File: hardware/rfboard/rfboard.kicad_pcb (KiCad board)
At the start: 4 copper layers, 20 x 59 mm, 62 parts, among them J1 10118194-0001LF, J2 Conn_01x04, J3 2337019-1, J4 Conn_01x02, P2 CONN_01X03, SW1 SW_Push, SW2 SW_Push, SW3 SW_Push, U1 STM32G070KBTx, U2 RFM69HCW, U3 CH340X, U4 XL-0807RGBC-WS2812B, U5 XC6206P332MR-G, U6 HX 1210-C06

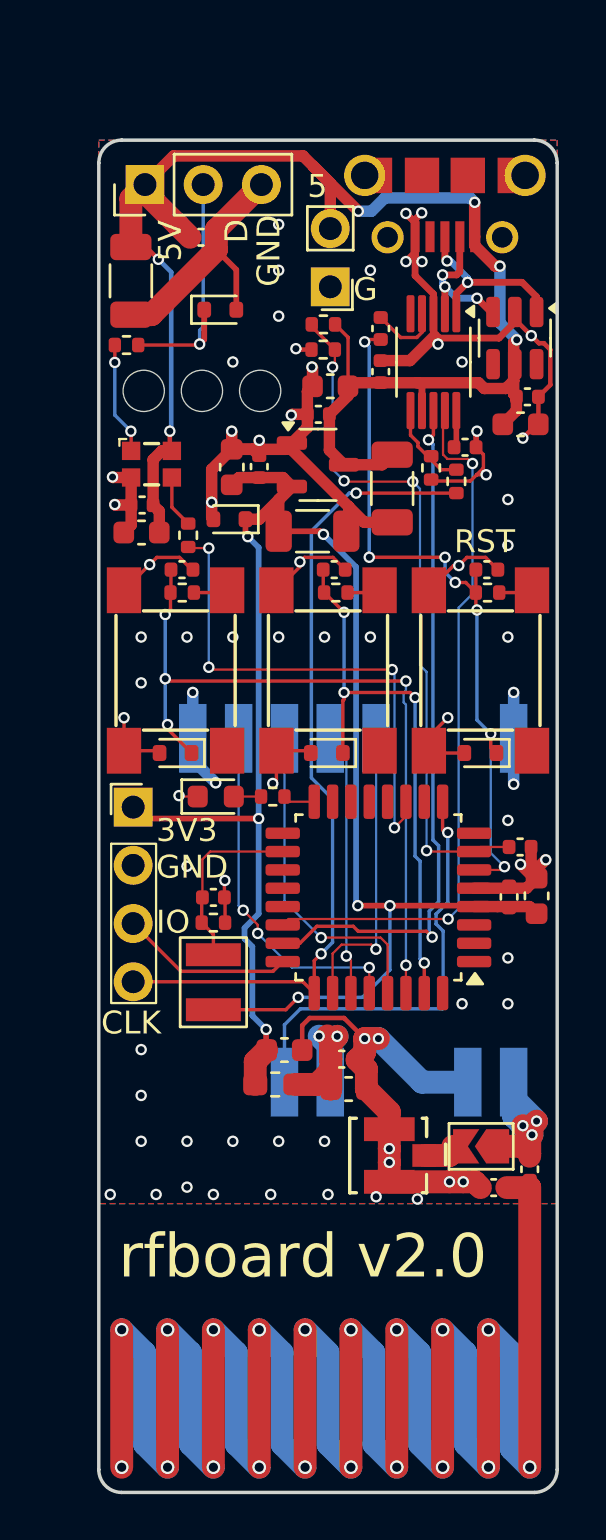
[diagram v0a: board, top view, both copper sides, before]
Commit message: Update the rfboard hardware designs for v2.1:
- Fix USB-USART connections to use the correct MCU pins
- Add thermal relief for the u.FL connector
- Switch to USB-C
- Switch to an LDO voltage regulator with a high PSRR
- Remove inner copper layers from antenna vias
- Increase antenna via copper to 1mm diameter
- Add a the 3rd pi filter footprint
- Add a 220uF electrolytic cap on the 5V rail
- Improve the decoupling story overall
- Remove the ferrite on the radio power supply

Change-Id: Iff05fab2d52248b6d165e85d5234a398977c2398
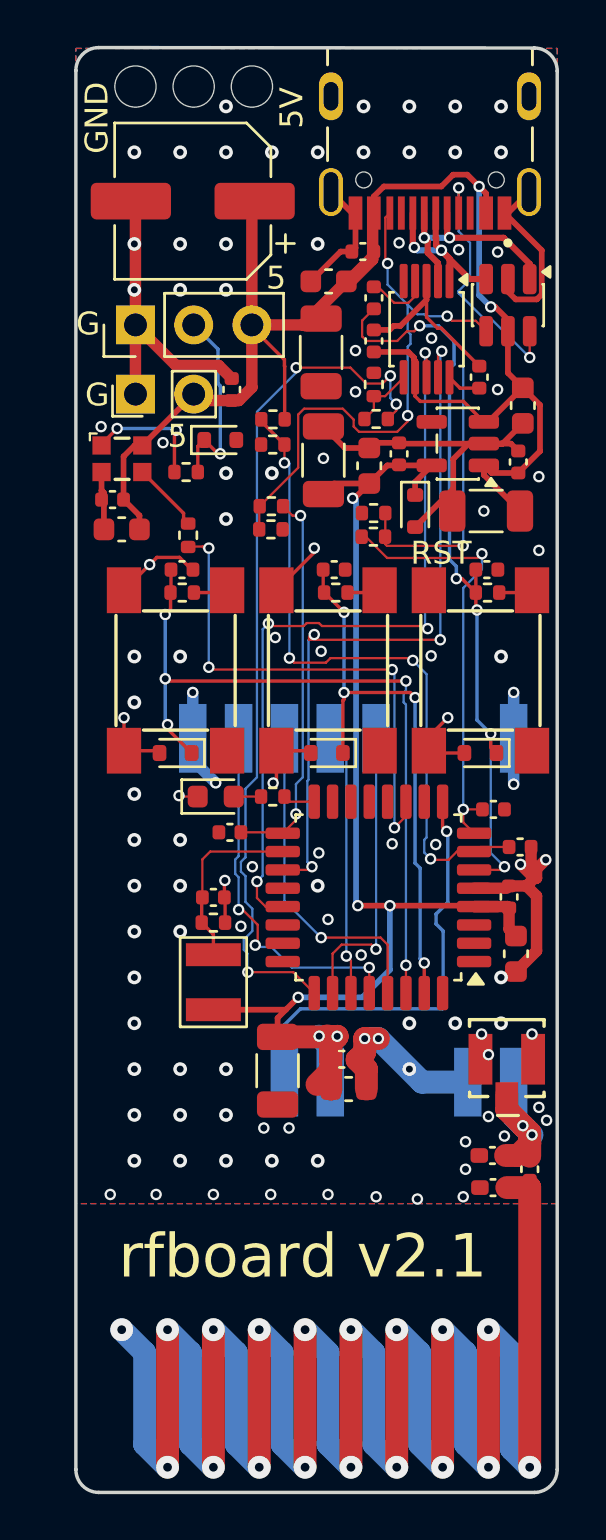
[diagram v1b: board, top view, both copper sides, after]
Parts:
- removed FB1: FerriteBead, Inductor_SMD:L_0603_1608Metric_Pad1.05x0.95mm_HandSolder
- removed J2: Conn_01x04, Homebrew:PinHeader_1x04_P2.54mm_Vertical_NoPlastic
- removed JP1: SolderJumper_2_Open, Jumper:SolderJumper-2_P1.3mm_Open_TrianglePad1.0x1.5mm
- added C27: 220uF, Capacitor_SMD:CP_Elec_6.3x5.8, F.Cu at (64.1, 91.7)
- added C28: 100nF, Capacitor_SMD:C_0402_1005Metric, F.Cu at (77.2, 118.2)
- added C29: 100nF, Capacitor_SMD:C_0402_1005Metric, F.Cu at (65.7, 119.2)
- added L2: 0, Inductor_SMD:L_0402_1005Metric_Pad0.77x0.64mm_HandSolder, F.Cu at (77.2, 133.3)
- added R12: 5k1, Resistor_SMD:R_0402_1005Metric, F.Cu at (72.0, 105.3)
- added R13: 10k, Resistor_SMD:R_0402_1005Metric, F.Cu at (72.0, 106.3)
- added R14: 5k1, Resistor_SMD:R_0402_1005Metric, F.Cu at (67.5, 106.0)
- added R15: 10k, Resistor_SMD:R_0402_1005Metric, F.Cu at (67.5, 105.0)
- C26: value 10uF -> 47uF; footprint Capacitor_SMD:C_0603_1608Metric -> Capacitor_SMD:C_1206_3216Metric
- C7: value 1pF -> 0R
- J1: footprint Homebrew:FRAMATOME_10118194-0001LF_fixed_bridges -> Homebrew:HRO_TYPE-C-31-M-12
- L1: value 10nH -> 0
- U5: value XC6206P332MR-G -> AP2112K-3.3; footprint Package_TO_SOT_SMD:SOT-23-3 -> Package_TO_SOT_SMD:SOT-23-5
- moved H3 13.3 mm to (64.1, 86.7), turned to 180 degrees
- moved C9 10.4 mm to (70.0, 95.2), turned to 180 degrees
- moved J4 9.70 mm to (61.6, 100.1), turned to 90 degrees
- moved C3 9.58 mm to (71.5, 93.9), turned to 180 degrees
- moved C11 8.96 mm to (78.3, 103.0), turned to 90 degrees
- moved C19 8.87 mm to (69.7, 98.3)
- moved C12 8.44 mm to (78.5, 100.6), turned to -90 degrees
- moved D4 8.11 mm to (73.8, 105.2), turned to -90 degrees
- moved C18 6.78 mm to (65.8, 99.9), turned to 90 degrees
- moved J3 6.70 mm to (77.8, 129.1), turned to 180 degrees
- moved U5 6.17 mm to (75.7, 102.2), turned to 180 degrees
- moved P2 6.14 mm to (61.6, 97.1)
- moved C13 6.13 mm to (73.1, 102.7)
- moved R5 6.12 mm to (63.8, 103.5)
- moved C14 6.00 mm to (71.8, 103.2)
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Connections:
- C20 pad 1: Net-(U2-3.3V) -> +3V3
- C26 pad 1: +3V3 -> GND
- C26 pad 2: GND -> +3V3
- C5 pad 1: Net-(U2-3.3V) -> +3V3
- C7 pad 2: Net-(JP1-A) -> /ANTENNA_UFL
- D3 pad 1: /USB_DP -> /USB_DN
- D3 pad 3: /USB_DN -> /USB_DP
- D3 pad 4: unconnected-(D3-IO3-Pad4) -> /CC2_RAW
- D3 pad 6: unconnected-(D3-IO4-Pad6) -> /CC1_RAW
- P2 pad 1: +5V -> GND
- P2 pad 3: GND -> +5V
- U1 pad 17: unconnected-(U1-PB2-Pad17) -> /CC2
- U1 pad 19: unconnected-(U1-NC/PA9-Pad19) -> /USART_TX
- U1 pad 21: unconnected-(U1-NC/PA10-Pad21) -> /USART_RX
- U1 pad 22: /USART_TX -> unconnected-(U1-PA9/PA11-Pad22)
- U1 pad 23: /USART_RX -> unconnected-(U1-PA10/PA12-Pad23)
- U1 pad 24: /SWDIO -> unconnected-(U1-PA13-Pad24)
- U1 pad 8: unconnected-(U1-PA1-Pad8) -> /CC1
- U2 pad 13: Net-(U2-3.3V) -> +3V3
- U2 pad 9: Net-(JP1-A) -> /ANTENNA_UFL
- U5 pad 1: GND -> +5V
- U5 pad 2: +3V3 -> GND
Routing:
- net /CC1_RAW: track 0.00 -> 27.5 mm, vias 0 -> 3
- net /CC2_RAW: track 0.00 -> 24.9 mm, vias 0 -> 3
- net GND: track 122.5 -> 98.4 mm, vias 73 -> 111
- net /CC1: track 0.00 -> 19.1 mm, vias 0 -> 2
- net +3V3: track 77.4 -> 59.7 mm, vias 7 -> 6
- net /CC2: track 0.00 -> 17.0 mm, vias 0 -> 2
- net Net-(U2-3.3V): track 9.78 -> 0.00 mm, vias 2 -> 0
- net Net-(JP1-A): track 7.68 -> 0.00 mm, vias 3 -> 0
- net /SWDIO: track 7.56 -> 0.00 mm
- net /ANTENNA: track 128.6 -> 122.6 mm, vias 19 -> 18
- net /ANTENNA_UFL: track 1.56 -> 7.52 mm, vias 0 -> 2
- net /USB_DN: track 6.53 -> 10.1 mm, vias 3 -> 2
- net /USART_RX: track 30.5 -> 34.0 mm, vias 2 -> 4
- net /LED_EXTERNAL: track 11.3 -> 8.56 mm
- net +5V: track 67.3 -> 69.2 mm, vias 6 -> 2
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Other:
- board size 20 x 59 mm -> 21 x 63 mm
- board text added: "915 MHz"
- board text added: "rfboard v2.1"
- board text removed: "3V3"
- board text removed: "CLK"
- board text removed: "D"
- board text removed: "IO"
- board text removed: "rfboard v2.0"
